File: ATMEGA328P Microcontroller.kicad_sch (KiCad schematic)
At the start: 24 parts, among them U1 24LC1025, U2 24LC1025, U3 ATmega328-P, U4 DS1337S_T_R, Y1 Crystal, Y2 Crystal

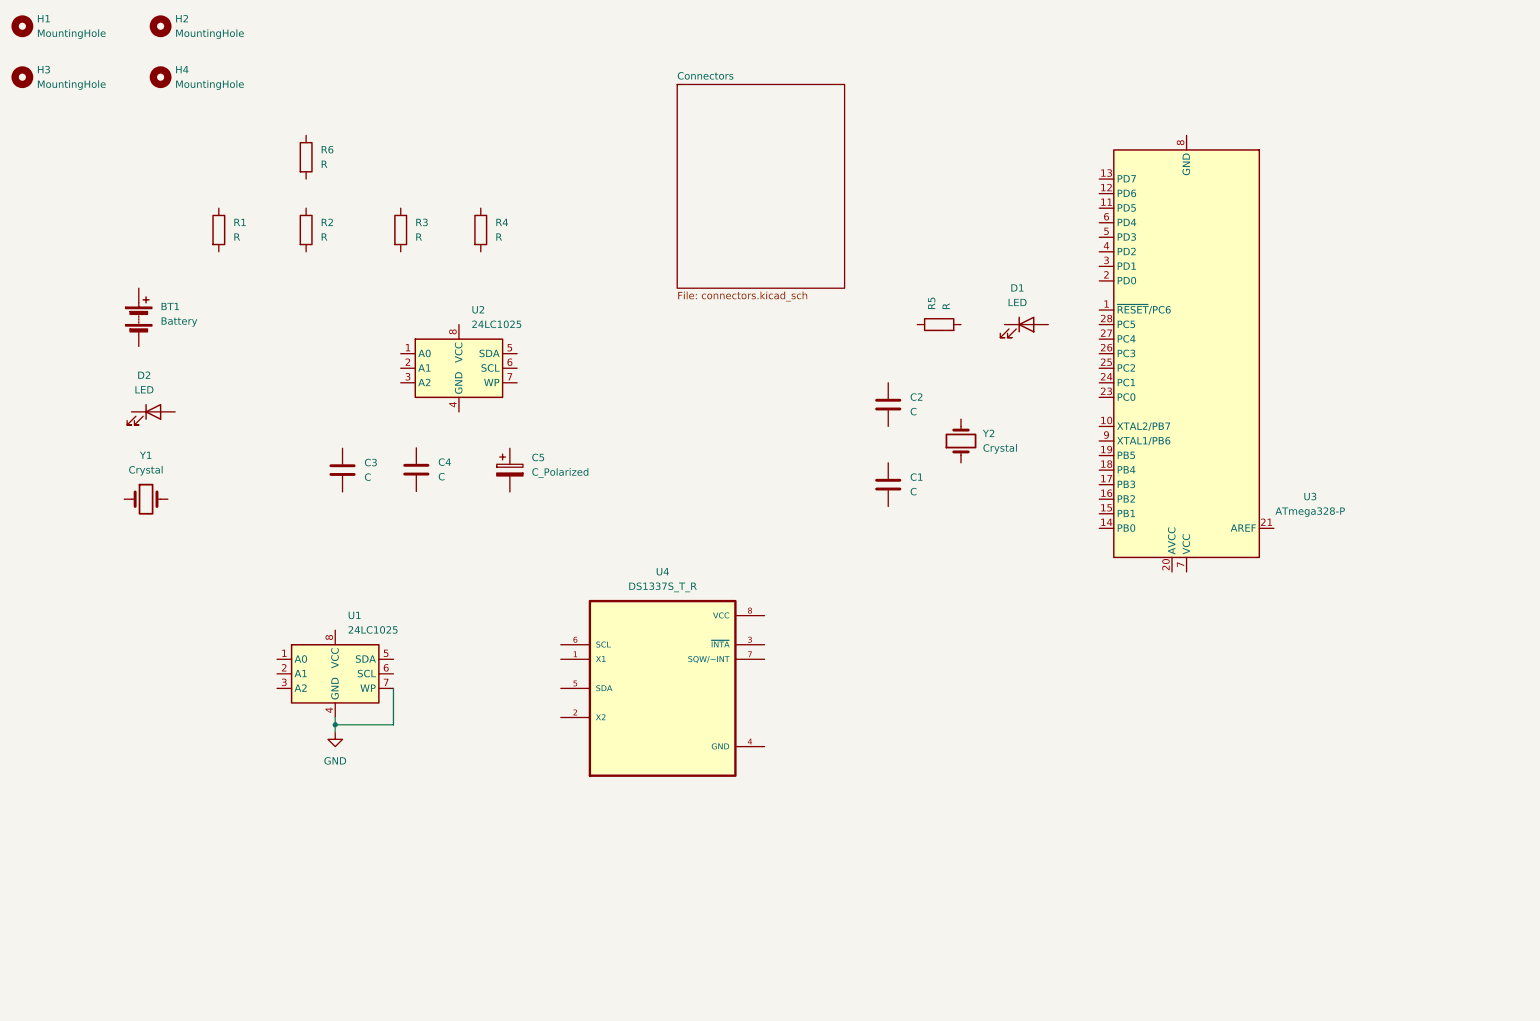
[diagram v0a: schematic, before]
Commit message: Arranged symbols in schematic
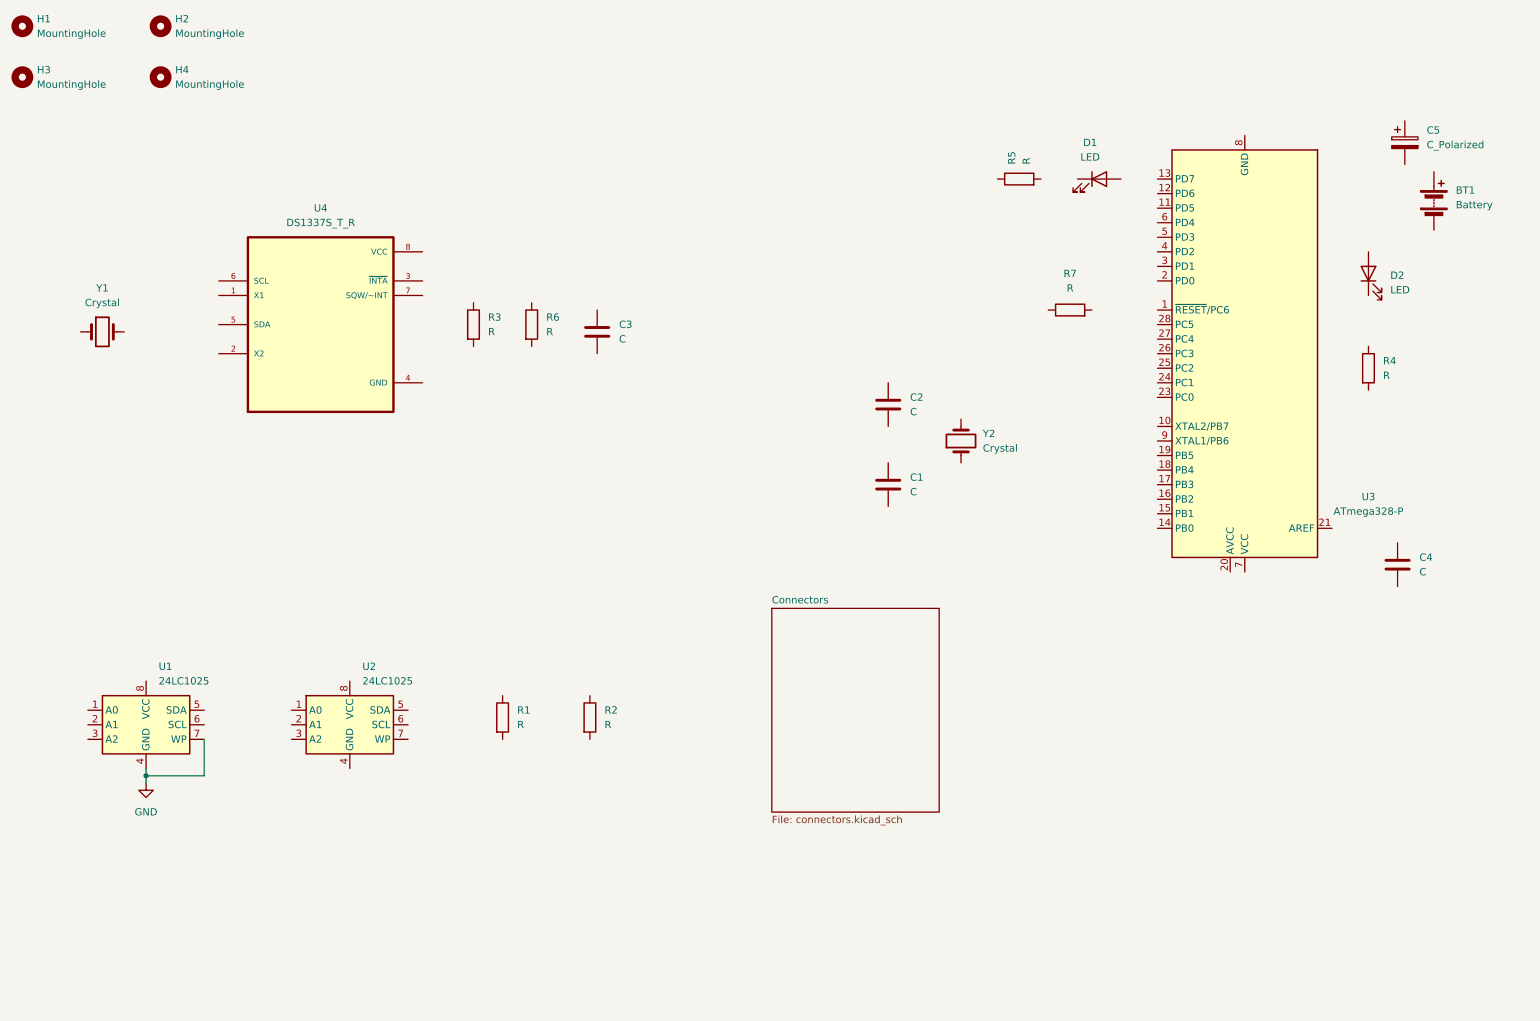
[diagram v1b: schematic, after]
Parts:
- added R7: R, symbol Device:R
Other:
- moved on the sheet: BT1, C3, C4, C5, D1, D2, R1, R2, R3, R4, R5, R6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

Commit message: Added values to components
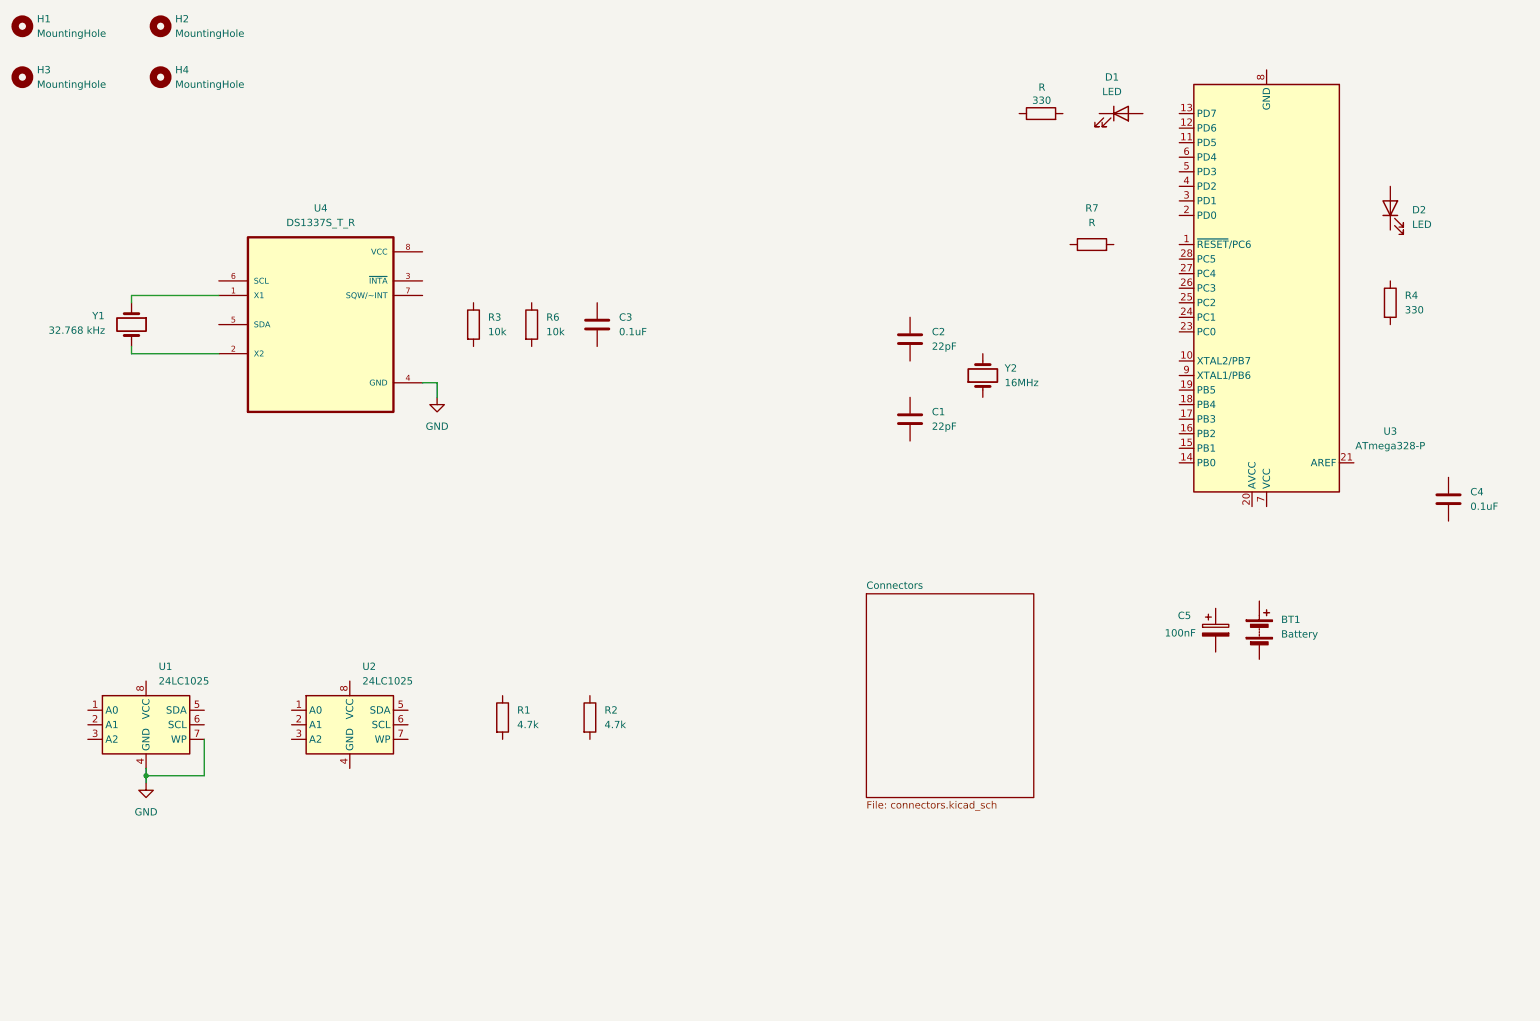
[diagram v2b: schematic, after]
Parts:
- C1, C2: value C -> 22pF
- C3, C4: value C -> 0.1uF
- C5: value C_Polarized -> 100nF
- R: renamed from R5; value R -> 330
- R1, R2: value R -> 4.7k
- R3, R6: value R -> 10k
- R4: value R -> 330
- Y1: value Crystal -> 32.768 kHz
- Y2: value Crystal -> 16MHz
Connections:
- net GND: now also U4.4 (GND)
- net at Y1.1: now also U4.1 (X1)
- net at Y1.2: now also U4.2 (X2)
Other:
- moved on the sheet: BT1, C1, C2, C3, C4, C5, D1, D2, R, R4, R7, U3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

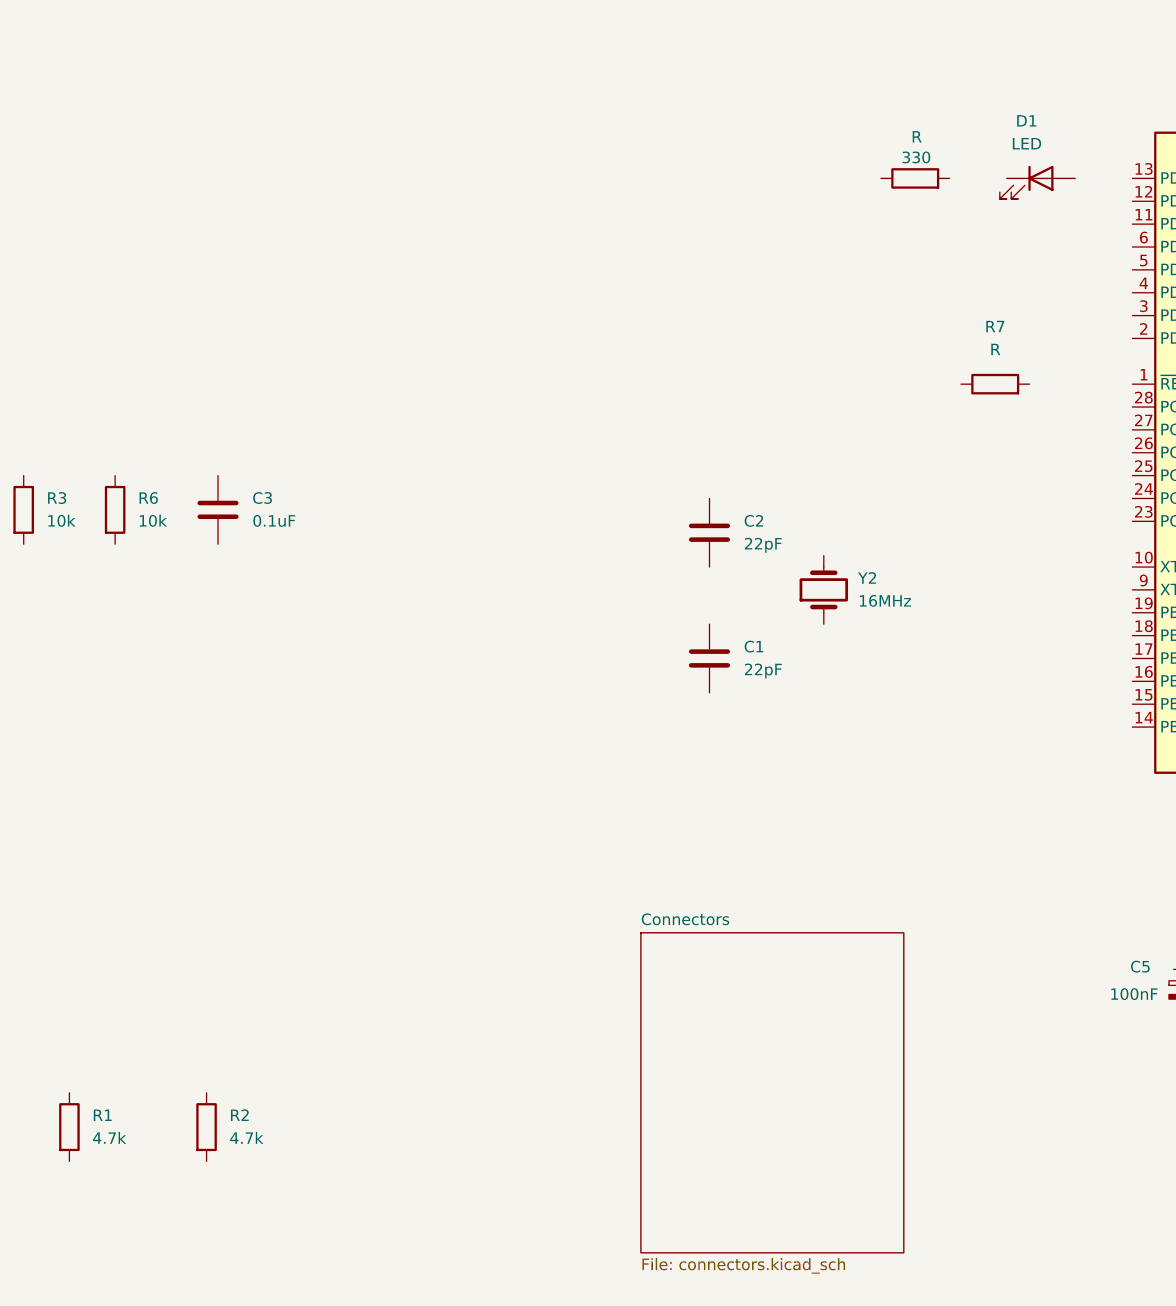
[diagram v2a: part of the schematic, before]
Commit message: Associated footprints
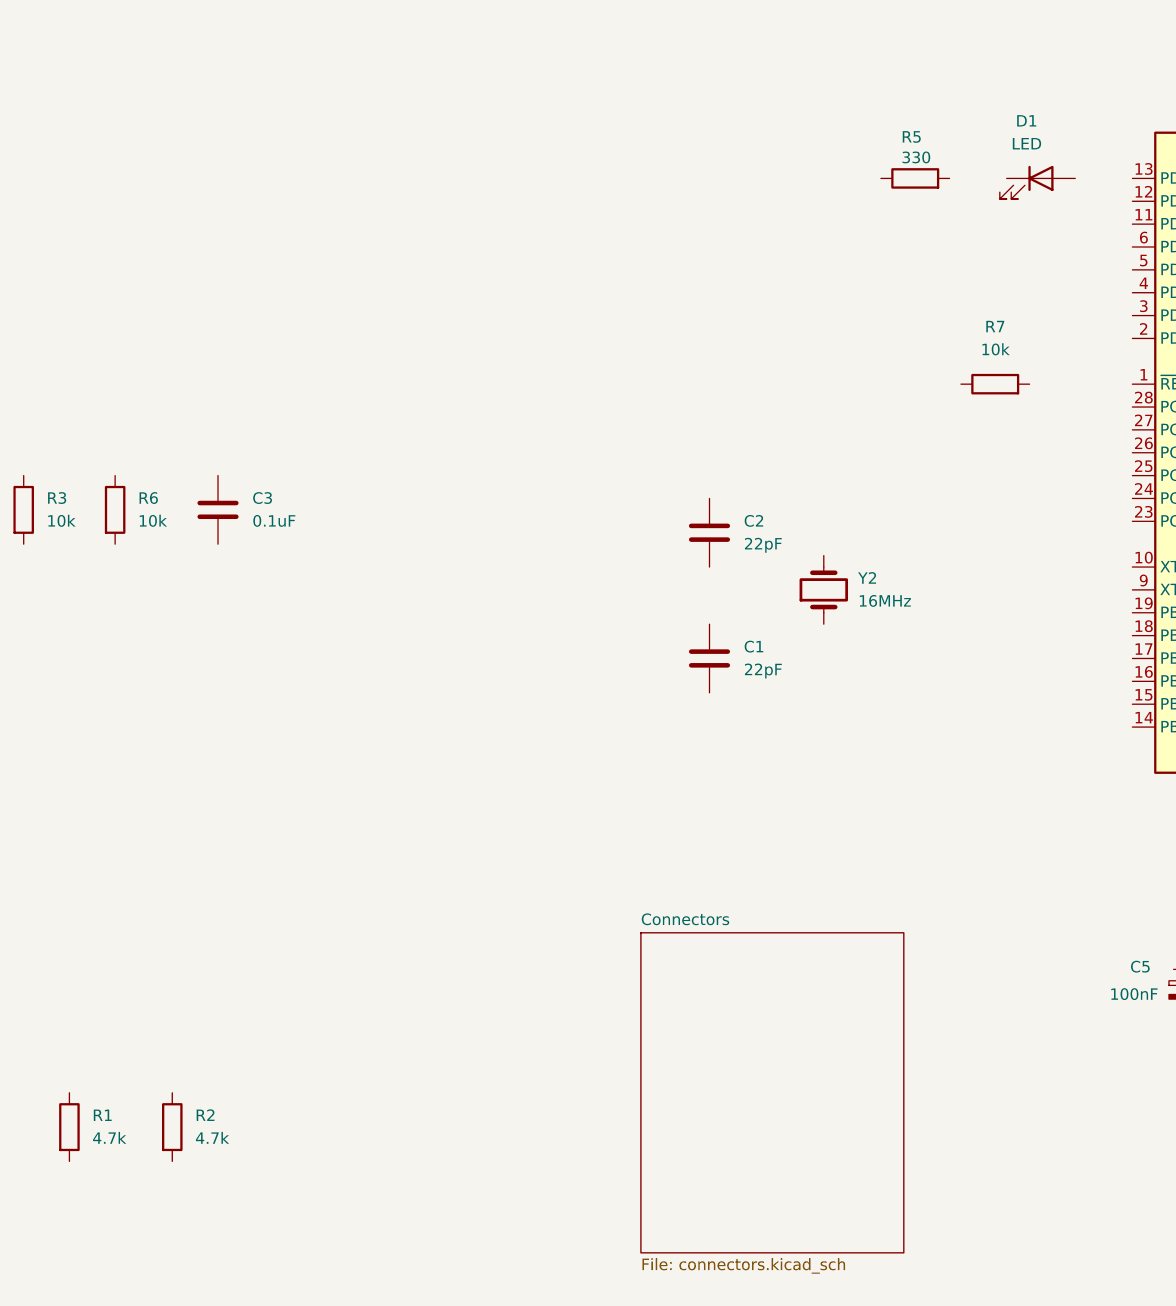
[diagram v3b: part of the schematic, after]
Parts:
- BT1: footprint (none) -> Connector_PinHeader_2.54mm:PinHeader_1x02_P2.54mm_Vertical
- C1, C2, C3, C4, C5: footprint (none) -> Capacitor_SMD:C_0805_2012Metric_Pad1.18x1.45mm_HandSolder
- D1, D2: footprint (none) -> LED_SMD:LED_0805_2012Metric
- H1, H2, H3, H4: footprint (none) -> MountingHole:MountingHole_2.1mm
- R1, R2, R3, R4, R6: footprint (none) -> Resistor_SMD:R_0805_2012Metric
- R5: renamed from R; footprint (none) -> Resistor_SMD:R_0805_2012Metric
- R7: value R -> 10k; footprint (none) -> Resistor_SMD:R_0805_2012Metric
- U1, U2: footprint (none) -> Package_SO:SOIC-8_5.23x5.23mm_P1.27mm
- Y1, Y2: footprint (none) -> Crystal:Crystal_SMD_5032-2Pin_5.0x3.2mm_HandSoldering
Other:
- moved on the sheet: R2
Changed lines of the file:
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@@
 			)
 		)
-		(property "Footprint" ""
+		(property "Footprint" "Crystal:Crystal_SMD_5032-2Pin_5.0x3.2mm_HandSoldering"
 			(at 39.37 72.39 0)
 			(effects
@@
 			)
 		)
-		(property "Footprint" ""
+		(property "Footprint" "LED_SMD:LED_0805_2012Metric"
 			(at 212.09 35.56 0)
 			(effects
@@
 			)
 		)
-		(property "Footprint" ""
+		(property "Footprint" "Resistor_SMD:R_0805_2012Metric"
 			(at 102.362 140.97 90)
 			(effects
@@
 			)
 		)
-		(property "Footprint" ""
+		(property "Footprint" "Capacitor_SMD:C_0805_2012Metric_Pad1.18x1.45mm_HandSolder"
 			(at 176.2252 92.71 0)
 			(effects
@@
 			)
 		)
-		(property "Footprint" ""
+		(property "Footprint" "Package_SO:SOIC-8_5.23x5.23mm_P1.27mm"
 			(at 41.91 142.24 0)
 			(effects
@@
 			)
 		)
-		(property "Footprint" ""
+		(property "Footprint" "MountingHole:MountingHole_2.1mm"
 			(at 44.45 20.32 0)
 			(effects
@@
 			)
 		)
-		(property "Footprint" ""
+		(property "Footprint" "LED_SMD:LED_0805_2012Metric"
 			(at 259.08 52.07 0)
 			(effects
@@
 			)
 		)
-		(property "Footprint" ""
+		(property "Footprint" "Capacitor_SMD:C_0805_2012Metric_Pad1.18x1.45mm_HandSolder"
 			(at 229.5652 129.54 0)
 			(effects
@@
 		(on_board yes)
 		(dnp no)
-		(property "Reference" "R"
+		(property "Reference" "R5"
 			(at 198.882 30.988 90)
 			(effects
@@
 			)
 		)
-		(property "Footprint" ""
+		(property "Footprint" "Resistor_SMD:R_0805_2012Metric"
 			(at 198.12 37.338 90)
 			(effects
@@
 			(project "ATMEGA328P Microcontroller"
 				(path "/af2a778c-0cbc-49a4-a908-0774f1699d74"
-					(reference "R")
+					(reference "R5")
 					(unit 1)
 				)
@@
 			)
 		)
-		(property "Footprint" ""
+		(property "Footprint" "Capacitor_SMD:C_0805_2012Metric_Pad1.18x1.45mm_HandSolder"
 			(at 121.6152 76.2 0)
 			(effects
@@
 			)
 		)
-		(property "Footprint" ""
+		(property "Footprint" "Resistor_SMD:R_0805_2012Metric"
 			(at 107.442 72.39 90)
 			(effects
@@
 			)
 		)
-		(property "Footprint" ""
+		(property "Footprint" "Crystal:Crystal_SMD_5032-2Pin_5.0x3.2mm_HandSoldering"
 			(at 187.96 81.28 0)
 			(effects
@@
 			)
 		)
-		(property "Footprint" ""
+		(property "Footprint" "Capacitor_SMD:C_0805_2012Metric_Pad1.18x1.45mm_HandSolder"
 			(at 270.2052 106.68 0)
 			(effects
@@
 			)
 		)
-		(property "Footprint" ""
+		(property "Footprint" "Resistor_SMD:R_0805_2012Metric"
 			(at 257.302 68.58 90)
 			(effects
@@
 			)
 		)
-		(property "Footprint" ""
+		(property "Footprint" "Resistor_SMD:R_0805_2012Metric"
 			(at 97.282 72.39 90)
 			(effects
@@
 			)
 		)
-		(property "Footprint" ""
+		(property "Footprint" "Capacitor_SMD:C_0805_2012Metric_Pad1.18x1.45mm_HandSolder"
 			(at 176.2252 78.74 0)
 			(effects
@@
 	(symbol
 		(lib_id "Device:R")
-		(at 119.38 140.97 0)
+		(at 115.57 140.97 0)
 		(unit 1)
 		(exclude_from_sim no)
@@
 		(fields_autoplaced yes)
 		(property "Reference" "R2"
-			(at 121.92 139.6999 0)
+			(at 118.11 139.6999 0)
 			(effects
 				(font
@@
 		)
 		(property "Value" "4.7k"
-			(at 121.92 142.2399 0)
-			(effects
-				(font
-					(size 1.27 1.27)
-				)
-				(justify left)
-			)
-		)
-		(property "Footprint" ""
-			(at 117.602 140.97 90)
-			(effects
-				(font
-					(size 1.27 1.27)
-				)
-				(hide yes)
-			)
-		)
-		(property "Datasheet" "~"
-			(at 119.38 140.97 0)
+			(at 118.11 142.2399 0)
+			(effects
+				(font
+					(size 1.27 1.27)
+				)
+				(justify left)
+			)
+		)
+		(property "Footprint" "Resistor_SMD:R_0805_2012Metric"
+			(at 113.792 140.97 90)
+			(effects
+				(font
+					(size 1.27 1.27)
+				)
+				(hide yes)
+			)
+		)
+		(property "Datasheet" "~"
+			(at 115.57 140.97 0)
 			(effects
 				(font
@@
 		)
 		(property "Description" "Resistor"
-			(at 119.38 140.97 0)
+			(at 115.57 140.97 0)
 			(effects
 				(font
@@
 			)
 		)
-		(property "Footprint" ""
+		(property "Footprint" "Package_SO:SOIC-8_5.23x5.23mm_P1.27mm"
 			(at 77.47 142.24 0)
 			(effects
@@
 			)
 		)
-		(property "Footprint" ""
+		(property "Footprint" "MountingHole:MountingHole_2.1mm"
 			(at 20.32 29.21 0)
 			(effects
@@
 			)
 		)
-		(property "Footprint" ""
+		(property "Footprint" "MountingHole:MountingHole_2.1mm"
 			(at 44.45 29.21 0)
 			(effects
@@
 			)
 		)
-		(property "Value" "R"
+		(property "Value" "10k"
 			(at 207.01 54.61 90)
 			(effects
@@
 			)
 		)
-		(property "Footprint" ""
+		(property "Footprint" "Resistor_SMD:R_0805_2012Metric"
 			(at 207.01 60.198 90)
 			(effects
@@
 			)
 		)
-		(property "Footprint" ""
+		(property "Footprint" "MountingHole:MountingHole_2.1mm"
 			(at 20.32 20.32 0)
 			(effects
@@
 			)
 		)
-		(property "Footprint" ""
+		(property "Footprint" "Connector_PinHeader_2.54mm:PinHeader_1x02_P2.54mm_Vertical"
 			(at 236.22 124.206 90)
 			(effects
